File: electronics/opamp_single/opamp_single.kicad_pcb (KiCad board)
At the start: 2 copper layers, 19 x 34 mm, 8 parts, among them J1 1, J2 2, J3 3, J4 4, J5 5, J6 6

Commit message: schematic and board completed
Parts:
- removed J2: 2, mill-max:PC_pin_nail_head_6092
- added C1: 100n, SquantorRcl:C-050_075-040X100, F.Cu at (149.8, 67.0)
- added U1: opamp_single_8pin, Package_DIP:DIP-8_W7.62mm_Socket, F.Cu at (146.0, 74.0)
- J1: value 1 -> -IN
- J3: value 3 -> +IN
- J4: value 4 -> V-
- J5: value 5 -> OUT
- J6: value 6 -> V+
- N1: value 20201120 -> V20201120
- moved N2 8.25 mm to (150.0, 86.2)
- moved N1 8.00 mm to (149.2, 90.0)
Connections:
- J3 pad 1: Net-(J1-Pad1) -> Net-(J3-Pad1)
- J4 pad 1: Net-(J1-Pad1) -> /V-
- J5 pad 1: Net-(J1-Pad1) -> Net-(J5-Pad1)
- J6 pad 1: Net-(J1-Pad1) -> /V+
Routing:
- net /V-: track 0.00 -> 35.6 mm
- net /V+: track 0.00 -> 23.8 mm
- net Net-(J3-Pad1): track 0.00 -> 17.2 mm
- net Net-(J1-Pad1): track 0.00 -> 16.9 mm
- net Net-(J5-Pad1): track 0.00 -> 3.83 mm

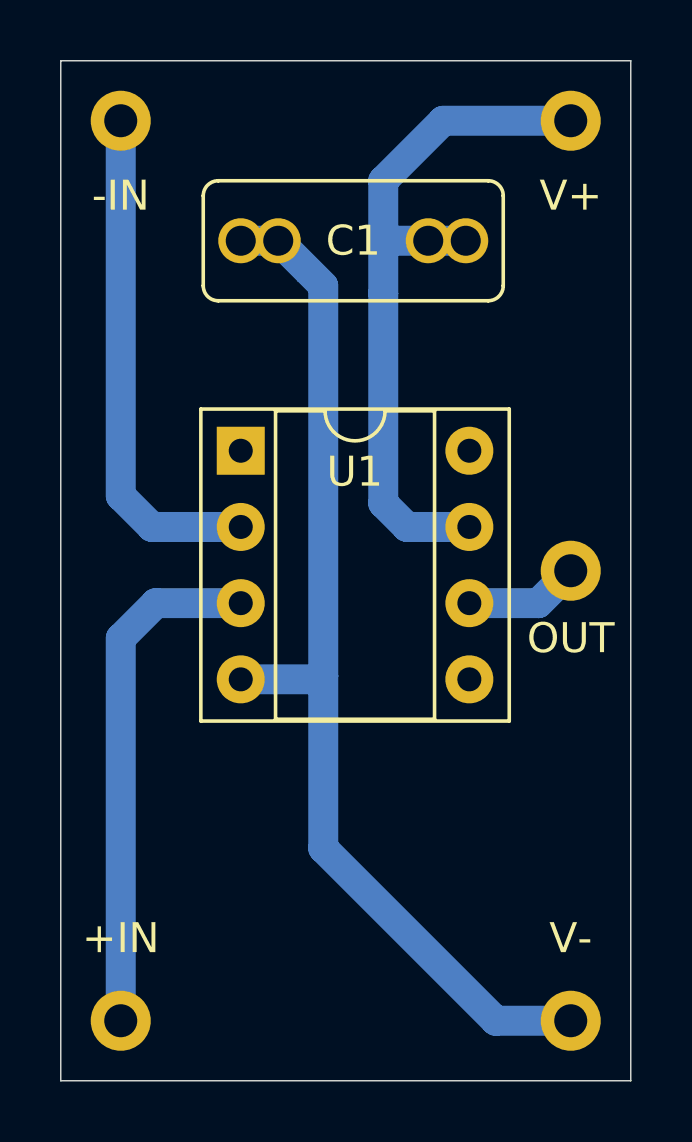
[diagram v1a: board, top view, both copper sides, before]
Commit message: completed silkscreen art
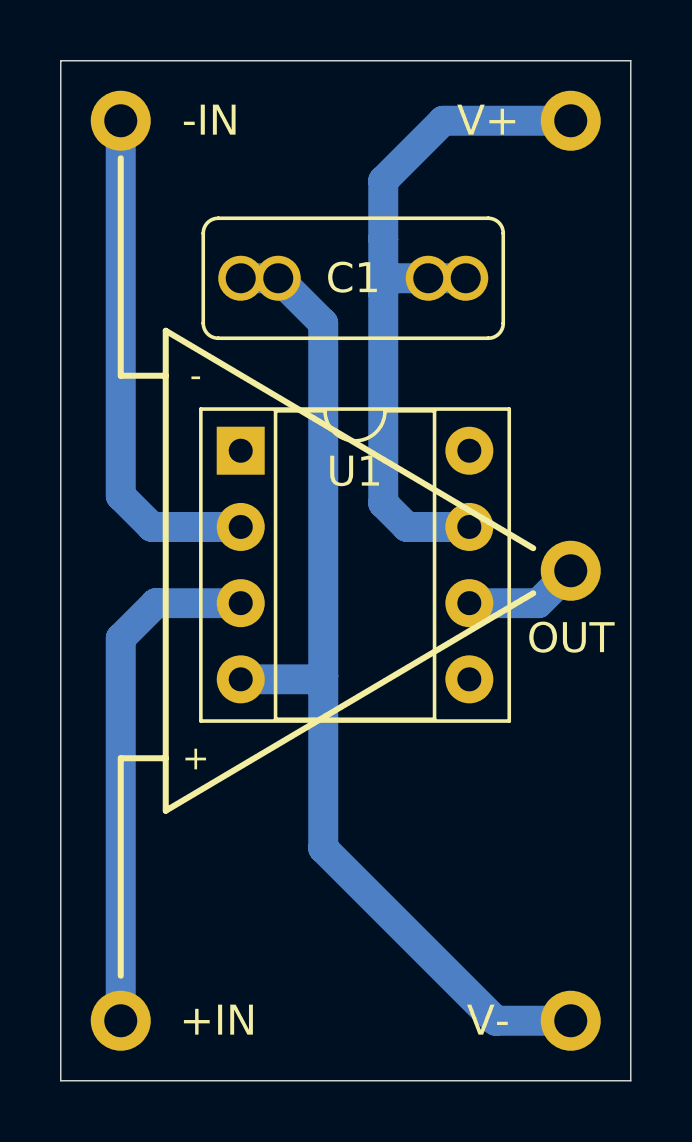
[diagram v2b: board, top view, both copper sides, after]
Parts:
- N1: value V20201120 -> V20201126
- moved C1 1.25 mm to (149.8, 68.2)
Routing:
- net /V-: track 35.6 -> 34.3 mm
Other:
- board text added: "+"
- board text added: "-"
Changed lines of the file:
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@@
   (general
     (thickness 1.6)
-    (drawings 4)
+    (drawings 13)
     (tracks 27)
     (zones 0)
@@
     (pcb_text_width 0.3)
     (pcb_text_size 1.5 1.5)
-    (mod_edge_width 0.12)
+    (mod_edge_width 0.2)
     (mod_text_size 0.8 0.8)
     (mod_text_width 0.12)
@@
   )
   (module SquantorRcl:C-050_075-040X100 (layer F.Cu)
-    (at 149.75 67)
+    (at 149.75 68.25)
     (descr "Through hole Film capacitor multipitch 5.0mm and 7.5mm size 4.0 by 10.0mm")
     (tags "Film capacitor multipitch")
@@
   (module mill-max:PC_pin_nail_head_6092 locked (layer F.Cu)
     (at 157 63)
-    (fp_text reference J6 (at 0 2.5) (layer F.Fab)
-      (effects (font (size 1 1) (thickness 0.15)))
-    )
-    (fp_text value V+ (at 0 2.5) (layer F.SilkS)
+    (fp_text reference J6 (at -3 0) (layer F.Fab)
+      (effects (font (size 1 1) (thickness 0.15)))
+    )
+    (fp_text value V+ (at -2.75 0) (layer F.SilkS)
       (effects (font (size 1 1) (thickness 0.15)))
     )
@@
   (module mill-max:PC_pin_nail_head_6092 locked (layer F.Cu)
     (at 157 93)
-    (fp_text reference J4 (at 0 -2.75) (layer F.Fab)
-      (effects (font (size 1 1) (thickness 0.15)))
-    )
-    (fp_text value V- (at 0 -2.75) (layer F.SilkS)
+    (fp_text reference J4 (at -2.75 0) (layer F.Fab)
+      (effects (font (size 1 1) (thickness 0.15)))
+    )
+    (fp_text value V- (at -2.75 0) (layer F.SilkS)
       (effects (font (size 1 1) (thickness 0.15)))
     )
@@
   (module mill-max:PC_pin_nail_head_6092 locked (layer F.Cu)
     (at 142 93)
-    (fp_text reference J3 (at 0 -2.75) (layer F.Fab)
-      (effects (font (size 1 1) (thickness 0.15)))
-    )
-    (fp_text value +IN (at 0 -2.75) (layer F.SilkS)
+    (fp_text reference J3 (at 3.25 0) (layer F.Fab)
+      (effects (font (size 1 1) (thickness 0.15)))
+    )
+    (fp_text value +IN (at 3.25 0) (layer F.SilkS)
       (effects (font (size 1 1) (thickness 0.15)))
     )
@@
   (module mill-max:PC_pin_nail_head_6092 locked (layer F.Cu)
     (at 142 63)
-    (fp_text reference J1 (at 0 2.5) (layer F.Fab)
-      (effects (font (size 1 1) (thickness 0.15)))
-    )
-    (fp_text value -IN (at 0 2.5) (layer F.SilkS)
+    (fp_text reference J1 (at 3 0) (layer F.Fab)
+      (effects (font (size 1 1) (thickness 0.15)))
+    )
+    (fp_text value -IN (at 3 0) (layer F.SilkS)
       (effects (font (size 1 1) (thickness 0.15)))
     )
@@
       (effects (font (size 1 1) (thickness 0.15)) (justify mirror))
     )
-    (fp_text value V20201120 (at 0.8 0.1) (layer B.SilkS)
+    (fp_text value V20201126 (at 0.8 0.1) (layer B.SilkS)
       (effects (font (size 0.8 0.8) (thickness 0.15)) (justify mirror))
     )
     (fp_line (start -0.5 -0.6) (end 0.5 -0.6) (layer B.SilkS) (width 0.15))
   )
+  (gr_line (start 142 84.25) (end 142 91.5) (layer F.SilkS) (width 0.2))
+  (gr_line (start 143.5 84.25) (end 142 84.25) (layer F.SilkS) (width 0.2))
+  (gr_line (start 142 71.5) (end 142 64.25) (layer F.SilkS) (width 0.2))
+  (gr_line (start 143.5 71.5) (end 142 71.5) (layer F.SilkS) (width 0.2))
+  (gr_line (start 143.5 70) (end 155.75 77.25) (layer F.SilkS) (width 0.2))
+  (gr_text + (at 144.5 84.25) (layer F.SilkS)
+    (effects (font (size 0.8 0.8) (thickness 0.12)))
+  )
+  (gr_text - (at 144.5 71.5) (layer F.SilkS)
+    (effects (font (size 0.8 0.8) (thickness 0.12)))
+  )
+  (gr_line (start 143.5 86) (end 155.75 78.75) (layer F.SilkS) (width 0.2))
+  (gr_line (start 143.5 70) (end 143.5 86) (layer F.SilkS) (width 0.2))
   (gr_line (start 159 61) (end 140 61) (layer Edge.Cuts) (width 0.05))
   (gr_line (start 159 61) (end 159 95) (layer Edge.Cuts) (width 0.05))
@@
   (segment (start 154.5 93) (end 148.75 87.25) (width 1) (layer B.Cu) (net 2))
   (segment (start 157 93) (end 154.5 93) (width 1) (layer B.Cu) (net 2))
-  (segment (start 147.25 67) (end 146 67) (width 1) (layer B.Cu) (net 2))
-  (segment (start 148.25 68) (end 147.25 67) (width 1) (layer B.Cu) (net 2))
-  (segment (start 148.75 68.5) (end 148.25 68) (width 1) (layer B.Cu) (net 2))
-  (segment (start 148.75 81.5) (end 148.75 68.5) (width 1) (layer B.Cu) (net 2))
+  (segment (start 146 68.25) (end 147.25 68.25) (width 1) (layer B.Cu) (net 2))
+  (segment (start 148.75 69.75) (end 147.25 68.25) (width 1) (layer B.Cu) (net 2))
+  (segment (start 148.75 81.5) (end 148.75 69.75) (width 1) (layer B.Cu) (net 2))
   (segment (start 146 79.08) (end 143.17 79.08) (width 1) (layer B.Cu) (net 3))
   (segment (start 142 80.25) (end 142 93) (width 1) (layer B.Cu) (net 3))
@@
   (segment (start 152.75 63) (end 150.75 65) (width 1) (layer B.Cu) (net 5))
   (segment (start 157 63) (end 152.75 63) (width 1) (layer B.Cu) (net 5))
-  (segment (start 153.5 67) (end 152.25 67) (width 1) (layer B.Cu) (net 5))
-  (segment (start 150.8 67) (end 150.75 66.95) (width 1) (layer B.Cu) (net 5))
-  (segment (start 152.25 67) (end 150.8 67) (width 1) (layer B.Cu) (net 5))
-  (segment (start 150.75 66.95) (end 150.75 68.75) (width 1) (layer B.Cu) (net 5))
   (segment (start 150.75 65) (end 150.75 66.95) (width 1) (layer B.Cu) (net 5))
+  (segment (start 153.5 68.25) (end 152.25 68.25) (width 1) (layer B.Cu) (net 5))
+  (segment (start 151 68.25) (end 150.75 68) (width 1) (layer B.Cu) (net 5))
+  (segment (start 152.25 68.25) (end 151 68.25) (width 1) (layer B.Cu) (net 5))
+  (segment (start 150.75 68) (end 150.75 68.75) (width 1) (layer B.Cu) (net 5))
+  (segment (start 150.75 66.95) (end 150.75 68) (width 1) (layer B.Cu) (net 5))
 )

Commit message: small schematic fixxes, updated versionnumber
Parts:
- N1: value V20201126 -> V20201128
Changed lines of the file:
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@@
   )
   (setup
-    (last_trace_width 1)
+    (last_trace_width 0.25)
     (user_trace_width 0.2)
     (user_trace_width 0.3)
@@
       (effects (font (size 1 1) (thickness 0.15)))
     )
+    (fp_line (start -4.5 2) (end 4.5 2) (layer F.SilkS) (width 0.12))
+    (fp_line (start 5 1.5) (end 5 -1.5) (layer F.SilkS) (width 0.12))
+    (fp_line (start 4.5 -2) (end -4.5 -2) (layer F.SilkS) (width 0.12))
+    (fp_line (start -5 -1.5) (end -5 1.5) (layer F.SilkS) (width 0.12))
+    (fp_line (start -5.5 -2.5) (end -5.5 2.5) (layer F.CrtYd) (width 0.025))
+    (fp_line (start -5.5 2.5) (end 5.5 2.5) (layer F.CrtYd) (width 0.025))
+    (fp_line (start 5.5 2.5) (end 5.5 -2.5) (layer F.CrtYd) (width 0.025))
+    (fp_line (start 5.5 -2.5) (end -5.5 -2.5) (layer F.CrtYd) (width 0.025))
     (fp_arc (start -4.5 -1.5) (end -4.5 -2) (angle -90) (layer F.SilkS) (width 0.12))
     (fp_arc (start 4.5 -1.5) (end 5 -1.5) (angle -90) (layer F.SilkS) (width 0.12))
     (fp_arc (start 4.5 1.5) (end 4.5 2) (angle -90) (layer F.SilkS) (width 0.12))
     (fp_arc (start -4.5 1.5) (end -5 1.5) (angle -90) (layer F.SilkS) (width 0.12))
-    (fp_line (start 5.5 -2.5) (end -5.5 -2.5) (layer F.CrtYd) (width 0.025))
-    (fp_line (start 5.5 2.5) (end 5.5 -2.5) (layer F.CrtYd) (width 0.025))
-    (fp_line (start -5.5 2.5) (end 5.5 2.5) (layer F.CrtYd) (width 0.025))
-    (fp_line (start -5.5 -2.5) (end -5.5 2.5) (layer F.CrtYd) (width 0.025))
-    (fp_line (start -5 -1.5) (end -5 1.5) (layer F.SilkS) (width 0.12))
-    (fp_line (start 4.5 -2) (end -4.5 -2) (layer F.SilkS) (width 0.12))
-    (fp_line (start 5 1.5) (end 5 -1.5) (layer F.SilkS) (width 0.12))
-    (fp_line (start -4.5 2) (end 4.5 2) (layer F.SilkS) (width 0.12))
     (pad 2 thru_hole circle (at 3.75 0) (size 1.5 1.5) (drill 1) (layers *.Cu *.Mask)
       (net 5 /V+))
@@
       (effects (font (size 1 1) (thickness 0.15)))
     )
+    (fp_line (start 9.15 -1.6) (end -1.55 -1.6) (layer F.CrtYd) (width 0.05))
+    (fp_line (start 9.15 9.2) (end 9.15 -1.6) (layer F.CrtYd) (width 0.05))
+    (fp_line (start -1.55 9.2) (end 9.15 9.2) (layer F.CrtYd) (width 0.05))
+    (fp_line (start -1.55 -1.6) (end -1.55 9.2) (layer F.CrtYd) (width 0.05))
+    (fp_line (start 8.95 -1.39) (end -1.33 -1.39) (layer F.SilkS) (width 0.12))
+    (fp_line (start 8.95 9.01) (end 8.95 -1.39) (layer F.SilkS) (width 0.12))
+    (fp_line (start -1.33 9.01) (end 8.95 9.01) (layer F.SilkS) (width 0.12))
+    (fp_line (start -1.33 -1.39) (end -1.33 9.01) (layer F.SilkS) (width 0.12))
+    (fp_line (start 6.46 -1.33) (end 4.81 -1.33) (layer F.SilkS) (width 0.12))
+    (fp_line (start 6.46 8.95) (end 6.46 -1.33) (layer F.SilkS) (width 0.12))
+    (fp_line (start 1.16 8.95) (end 6.46 8.95) (layer F.SilkS) (width 0.12))
+    (fp_line (start 1.16 -1.33) (end 1.16 8.95) (layer F.SilkS) (width 0.12))
+    (fp_line (start 2.81 -1.33) (end 1.16 -1.33) (layer F.SilkS) (width 0.12))
+    (fp_line (start 8.89 -1.33) (end -1.27 -1.33) (layer F.Fab) (width 0.1))
+    (fp_line (start 8.89 8.95) (end 8.89 -1.33) (layer F.Fab) (width 0.1))
+    (fp_line (start -1.27 8.95) (end 8.89 8.95) (layer F.Fab) (width 0.1))
+    (fp_line (start -1.27 -1.33) (end -1.27 8.95) (layer F.Fab) (width 0.1))
+    (fp_line (start 0.635 -0.27) (end 1.635 -1.27) (layer F.Fab) (width 0.1))
+    (fp_line (start 0.635 8.89) (end 0.635 -0.27) (layer F.Fab) (width 0.1))
+    (fp_line (start 6.985 8.89) (end 0.635 8.89) (layer F.Fab) (width 0.1))
+    (fp_line (start 6.985 -1.27) (end 6.985 8.89) (layer F.Fab) (width 0.1))
+    (fp_line (start 1.635 -1.27) (end 6.985 -1.27) (layer F.Fab) (width 0.1))
     (fp_text user %R (at 3.81 3.81) (layer F.Fab)
       (effects (font (size 1 1) (thickness 0.15)))
     )
     (fp_arc (start 3.81 -1.33) (end 2.81 -1.33) (angle -180) (layer F.SilkS) (width 0.12))
-    (fp_line (start 1.635 -1.27) (end 6.985 -1.27) (layer F.Fab) (width 0.1))
-    (fp_line (start 6.985 -1.27) (end 6.985 8.89) (layer F.Fab) (width 0.1))
-    (fp_line (start 6.985 8.89) (end 0.635 8.89) (layer F.Fab) (width 0.1))
-    (fp_line (start 0.635 8.89) (end 0.635 -0.27) (layer F.Fab) (width 0.1))
-    (fp_line (start 0.635 -0.27) (end 1.635 -1.27) (layer F.Fab) (width 0.1))
-    (fp_line (start -1.27 -1.33) (end -1.27 8.95) (layer F.Fab) (width 0.1))
-    (fp_line (start -1.27 8.95) (end 8.89 8.95) (layer F.Fab) (width 0.1))
-    (fp_line (start 8.89 8.95) (end 8.89 -1.33) (layer F.Fab) (width 0.1))
-    (fp_line (start 8.89 -1.33) (end -1.27 -1.33) (layer F.Fab) (width 0.1))
-    (fp_line (start 2.81 -1.33) (end 1.16 -1.33) (layer F.SilkS) (width 0.12))
-    (fp_line (start 1.16 -1.33) (end 1.16 8.95) (layer F.SilkS) (width 0.12))
-    (fp_line (start 1.16 8.95) (end 6.46 8.95) (layer F.SilkS) (width 0.12))
-    (fp_line (start 6.46 8.95) (end 6.46 -1.33) (layer F.SilkS) (width 0.12))
-    (fp_line (start 6.46 -1.33) (end 4.81 -1.33) (layer F.SilkS) (width 0.12))
-    (fp_line (start -1.33 -1.39) (end -1.33 9.01) (layer F.SilkS) (width 0.12))
-    (fp_line (start -1.33 9.01) (end 8.95 9.01) (layer F.SilkS) (width 0.12))
-    (fp_line (start 8.95 9.01) (end 8.95 -1.39) (layer F.SilkS) (width 0.12))
-    (fp_line (start 8.95 -1.39) (end -1.33 -1.39) (layer F.SilkS) (width 0.12))
-    (fp_line (start -1.55 -1.6) (end -1.55 9.2) (layer F.CrtYd) (width 0.05))
-    (fp_line (start -1.55 9.2) (end 9.15 9.2) (layer F.CrtYd) (width 0.05))
-    (fp_line (start 9.15 9.2) (end 9.15 -1.6) (layer F.CrtYd) (width 0.05))
-    (fp_line (start 9.15 -1.6) (end -1.55 -1.6) (layer F.CrtYd) (width 0.05))
     (pad 8 thru_hole oval (at 7.62 0) (size 1.6 1.6) (drill 0.8) (layers *.Cu *.Mask)
       (net 6 "Net-(U1-Pad8)"))
@@
       (effects (font (size 1 1) (thickness 0.15)))
     )
-    (fp_circle (center 0 0) (end 1.3 0) (layer F.CrtYd) (width 0.025))
-    (fp_circle (center 0 0) (end 1.3 0) (layer B.CrtYd) (width 0.025))
+    (fp_circle (center 0 0) (end 1.3 0) (layer B.CrtYd) (width 0.025))
+    (fp_circle (center 0 0) (end 1.3 0) (layer F.CrtYd) (width 0.025))
     (pad 1 thru_hole circle (at 0 0) (size 2 2) (drill 1.1) (layers *.Cu *.Mask)
       (net 5 /V+))
@@
       (effects (font (size 1 1) (thickness 0.15)))
     )
-    (fp_circle (center 0 0) (end 1.3 0) (layer F.CrtYd) (width 0.025))
-    (fp_circle (center 0 0) (end 1.3 0) (layer B.CrtYd) (width 0.025))
+    (fp_circle (center 0 0) (end 1.3 0) (layer B.CrtYd) (width 0.025))
+    (fp_circle (center 0 0) (end 1.3 0) (layer F.CrtYd) (width 0.025))
     (pad 1 thru_hole circle (at 0 0) (size 2 2) (drill 1.1) (layers *.Cu *.Mask)
       (net 4 "Net-(J5-Pad1)"))
@@
       (effects (font (size 1 1) (thickness 0.15)))
     )
-    (fp_circle (center 0 0) (end 1.3 0) (layer B.CrtYd) (width 0.025))
-    (fp_circle (center 0 0) (end 1.3 0) (layer F.CrtYd) (width 0.025))
+    (fp_circle (center 0 0) (end 1.3 0) (layer F.CrtYd) (width 0.025))
+    (fp_circle (center 0 0) (end 1.3 0) (layer B.CrtYd) (width 0.025))
     (pad 1 thru_hole circle (at 0 0) (size 2 2) (drill 1.1) (layers *.Cu *.Mask)
       (net 2 /V-))
@@
       (effects (font (size 1 1) (thickness 0.15)))
     )
-    (fp_circle (center 0 0) (end 1.3 0) (layer B.CrtYd) (width 0.025))
-    (fp_circle (center 0 0) (end 1.3 0) (layer F.CrtYd) (width 0.025))
+    (fp_circle (center 0 0) (end 1.3 0) (layer F.CrtYd) (width 0.025))
+    (fp_circle (center 0 0) (end 1.3 0) (layer B.CrtYd) (width 0.025))
     (pad 1 thru_hole circle (at 0 0) (size 2 2) (drill 1.1) (layers *.Cu *.Mask)
       (net 3 "Net-(J3-Pad1)"))
@@
       (effects (font (size 1 1) (thickness 0.15)))
     )
-    (fp_circle (center 0 0) (end 1.3 0) (layer B.CrtYd) (width 0.025))
-    (fp_circle (center 0 0) (end 1.3 0) (layer F.CrtYd) (width 0.025))
+    (fp_circle (center 0 0) (end 1.3 0) (layer F.CrtYd) (width 0.025))
+    (fp_circle (center 0 0) (end 1.3 0) (layer B.CrtYd) (width 0.025))
     (pad 1 thru_hole circle (at 0 0) (size 2 2) (drill 1.1) (layers *.Cu *.Mask)
       (net 1 "Net-(J1-Pad1)"))
@@
       (effects (font (size 1 1) (thickness 0.15)) (justify mirror))
     )
-    (fp_text value V20201126 (at 0.8 0.1) (layer B.SilkS)
+    (fp_text value V20201128 (at 0.8 0.1) (layer B.SilkS)
       (effects (font (size 0.8 0.8) (thickness 0.15)) (justify mirror))
     )
